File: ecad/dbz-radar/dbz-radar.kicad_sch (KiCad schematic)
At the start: 139 parts, among them J1 B2B-PH-SM4-TB, J2 USB4220-03-0880-C, J3 F300-1B7H1-11040-E100, J4 533980271, Q1 Q_PMOS, SW1 SW_Push, SW2 SW_Push, U1 USBLC6-2SC6, U2 TPS61169, U3 MCP738311/2, U4 MAX17048/9, U5 AP2112K-3.3, U6 PCA9554, U7 MAX98357A, U8 ESP32-S3-WROOM-1

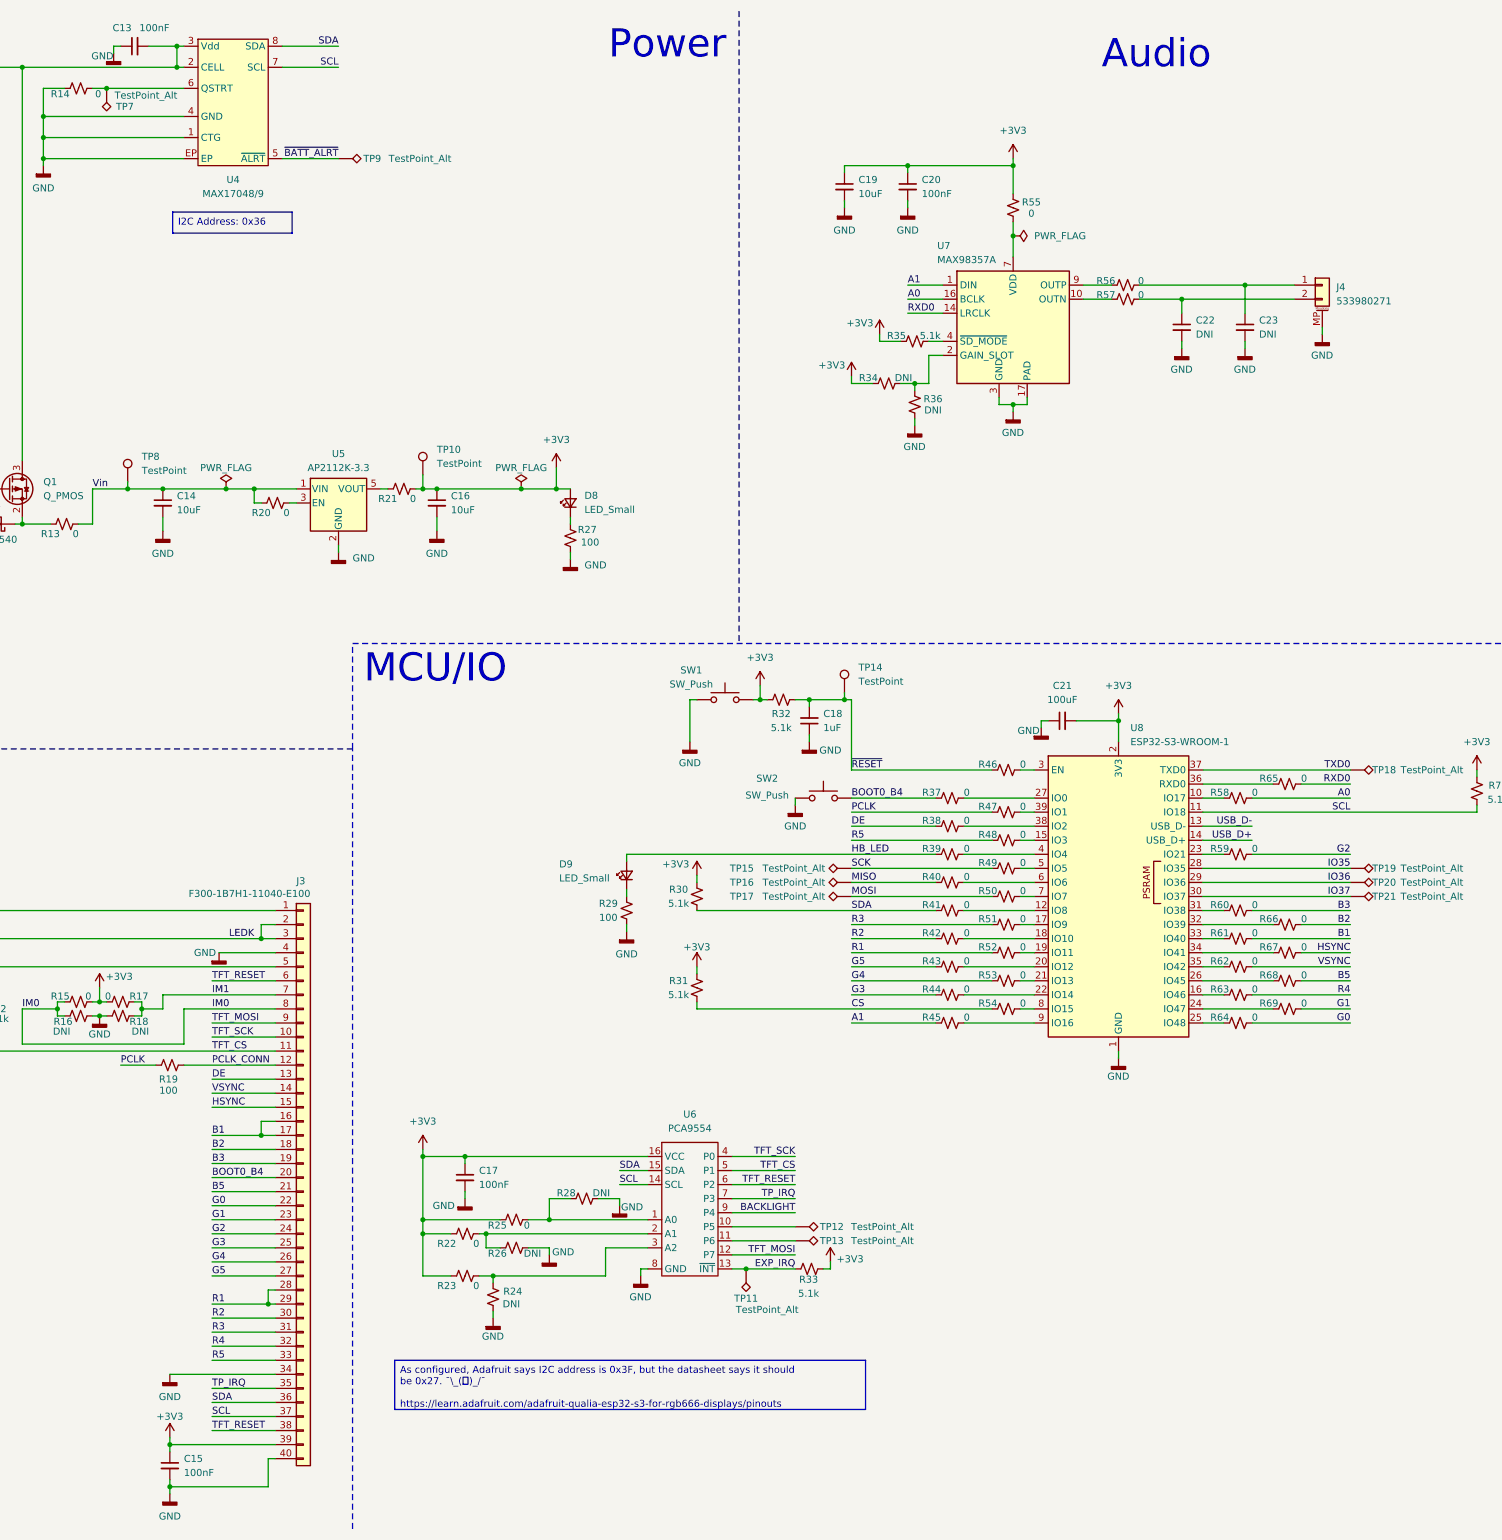
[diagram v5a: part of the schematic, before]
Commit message: added all footprints, some 3D models missing
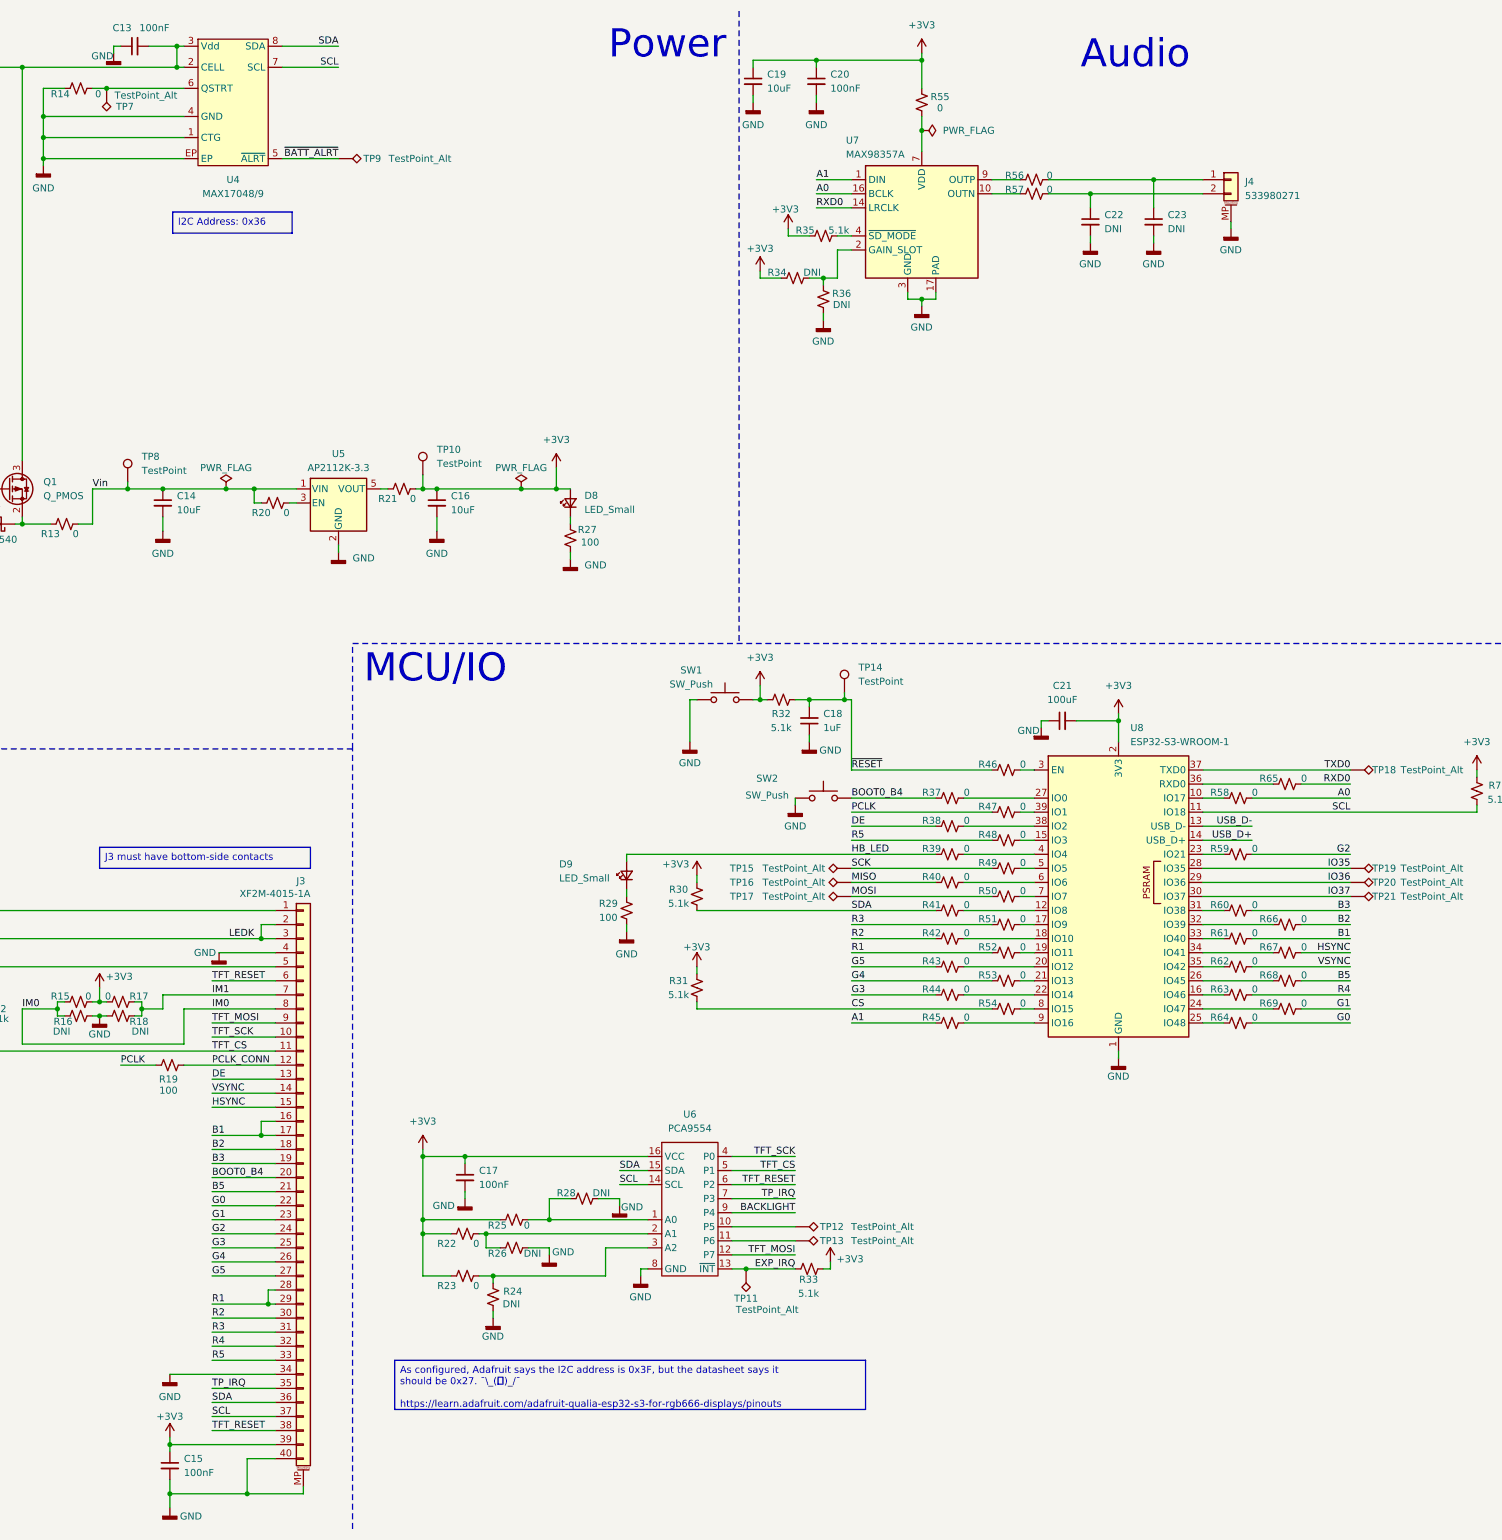
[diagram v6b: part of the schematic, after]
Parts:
- J3: value F300-1B7H1-11040-E100 -> XF2M-4015-1A; footprint (none) -> Connector_FFC-FPC:Omron_XF2M-4015-1A_1x40-1MP_P0.5mm_Horizontal; symbol Connector_Generic:Conn_01x40 -> Connector_Generic_MountingPin:Conn_01x40_MountingPin
- J4: footprint (none) -> Connector_Molex:Molex_PicoBlade_53398-0271_1x02-1MP_P1.25mm_Vertical
- U1: footprint Package_TO_SOT_SMD:SOT-23-6 -> Package_TO_SOT_SMD:SOT-23-6_Handsoldering
- U5: footprint Package_TO_SOT_SMD:SOT-23-5 -> Package_TO_SOT_SMD:SOT-23-5_HandSoldering
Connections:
- net GND: now also J3.MP (MountPin)
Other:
- moved on the sheet: C19, C20, C22, C23, J4, R34, R35, R36, R55, R56, R57, U7

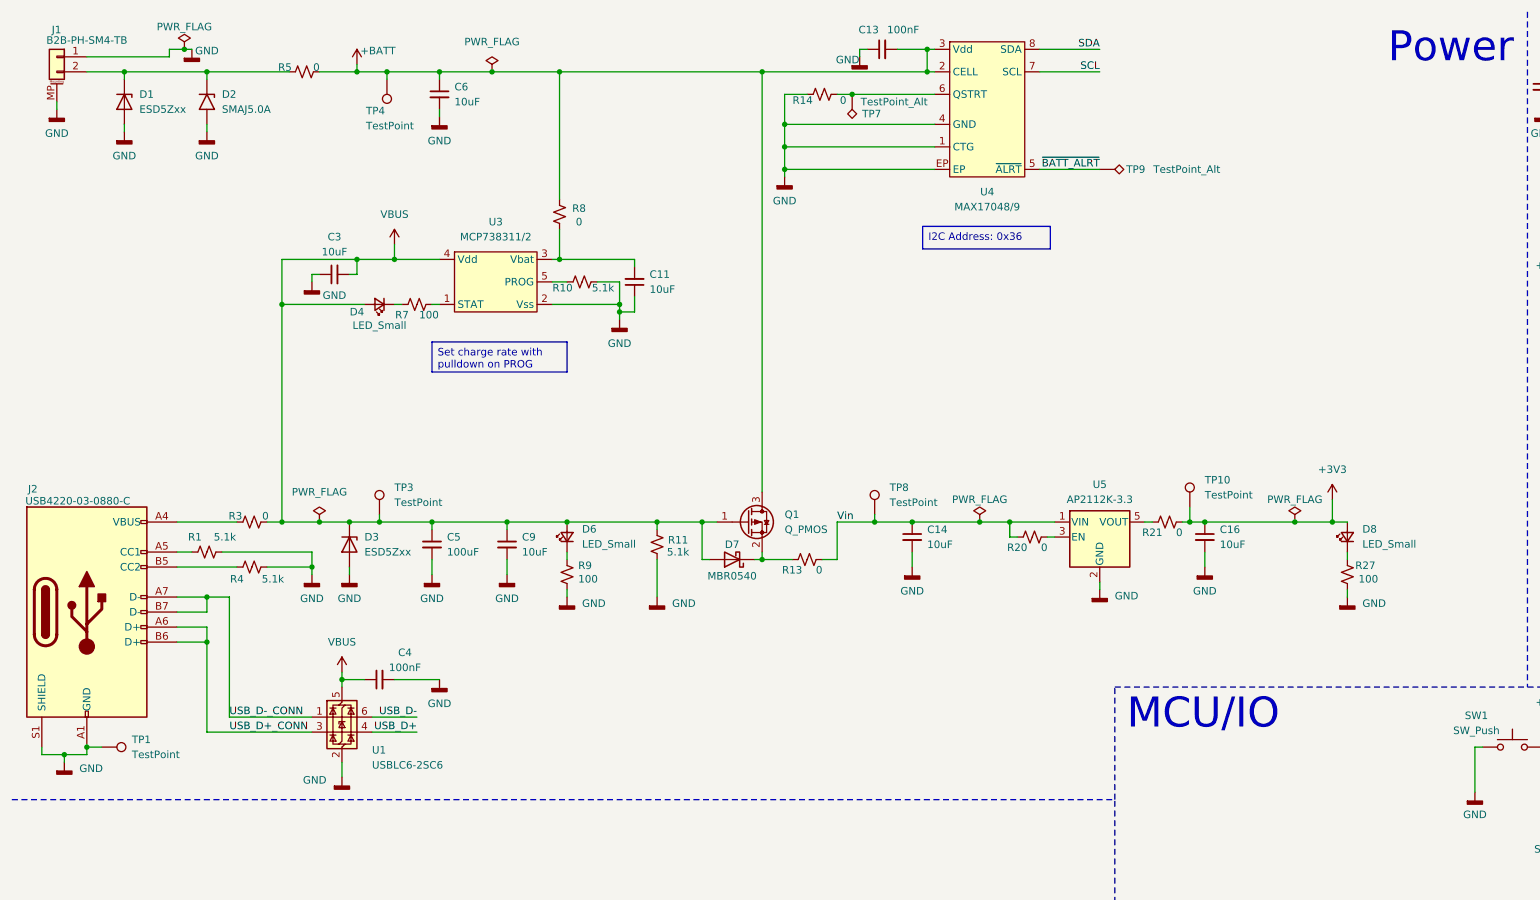
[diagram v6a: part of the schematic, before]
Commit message: match USB4220 symbol, footprint, and add 3D
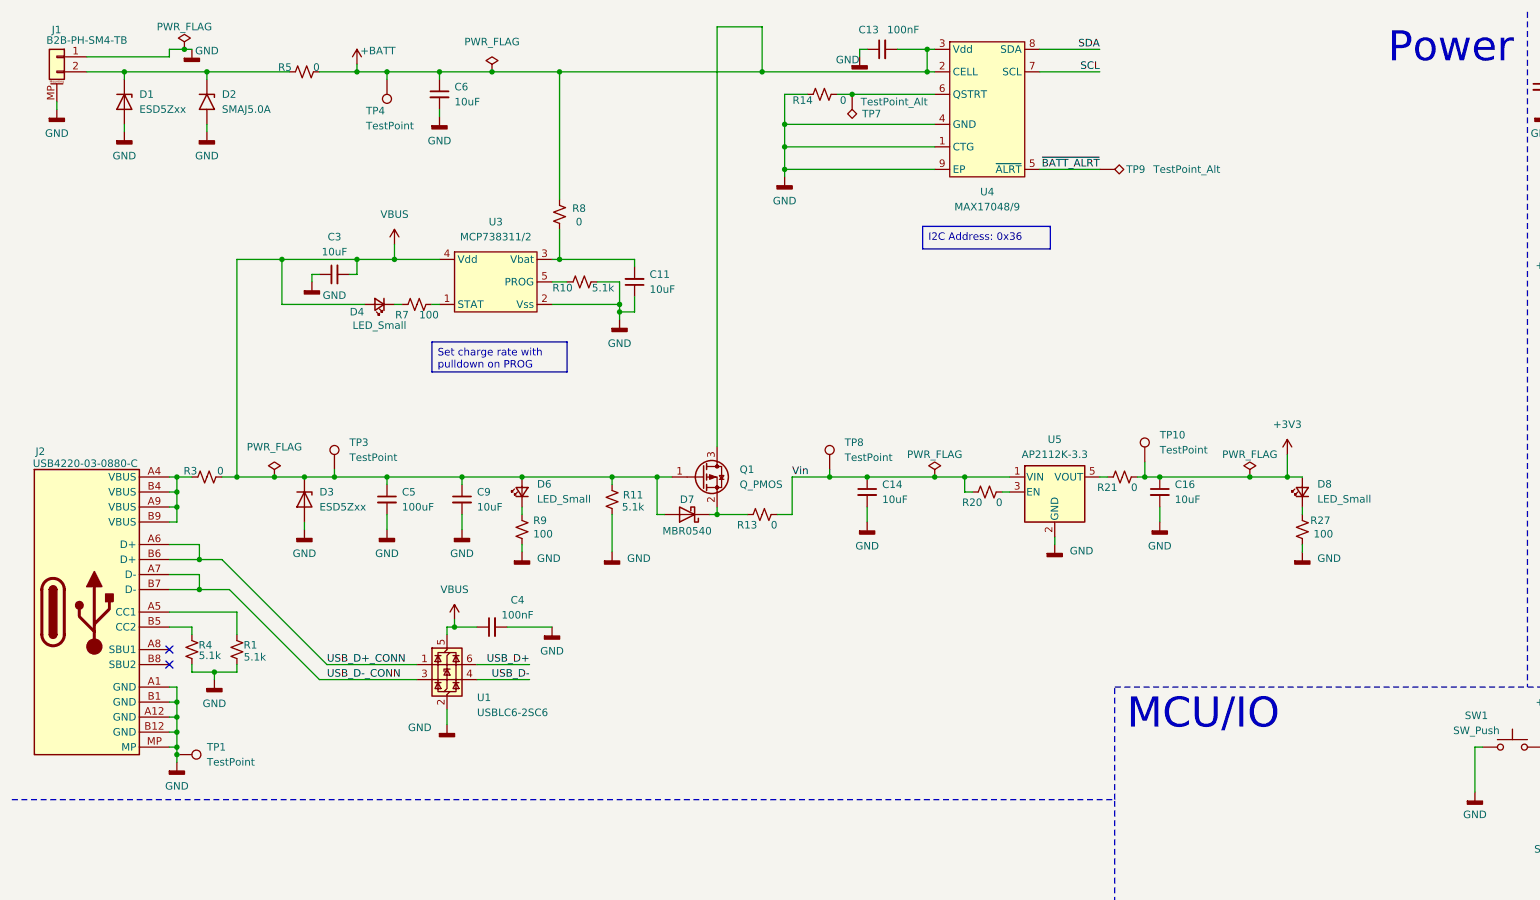
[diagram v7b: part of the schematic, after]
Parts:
- J2: symbol Connector:USB_C_Receptacle_USB2.0_14P -> USB4220-03:USB4220
- U2: footprint Package_TO_SOT_SMD:SOT-353_SC-70-5_Handsoldering -> Package_TO_SOT_SMD:SOT-353_SC-70-5
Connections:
- net GND: now also J2.MP, R1.1, R4.1, U4.9 (EP); no longer J2.S1 (SHIELD), R1.2, R4.2, U4.EP
- net USB_D+: now also U1.6 (I/O1); no longer U1.4 (I/O2)
- net USB_D+_CONN: now also U1.1 (I/O1); no longer U1.3 (I/O2)
- net USB_D-: now also U1.4 (I/O2); no longer U1.6 (I/O1)
- net USB_D-_CONN: now also U1.3 (I/O2); no longer U1.1 (I/O1)
- net at J2.B5 (CC2): now also R4.2; no longer R4.1
- net at J2.A5 (CC1): now also R1.2; no longer R1.1
- no-connect marks 0 -> 2
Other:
- moved on the sheet: C14, C16, C4, C5, C9, D3, D6, D7, D8, Q1, R1, R11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

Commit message: add user button symbol and footprints to layout
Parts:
- removed TP13: TestPoint_Alt, TestPoint:TestPoint_THTPad_D2.5mm_Drill1.2mm, symbol Connector:TestPoint_Alt
- added C24: 100nF, Capacitor_SMD:C_0805_2012Metric_Pad1.18x1.45mm_HandSolder, symbol Device:C_Small
- added FID1, FID2, FID3: Fiducial, Fiducial:Fiducial_1mm_Mask2mm, symbol Mechanical:Fiducial
- added H1, H2, H3, H4, H5, H6: MountingHole_Pad, M1:M1-mounting-hole, symbol Mechanical:MountingHole_Pad
- added R71: 5.1k, Resistor_SMD:R_0805_2012Metric_Pad1.20x1.40mm_HandSolder, symbol Device:R_Small_US
- added SW3: 1-825027-7, 1-825027-7:1-825027-7, symbol 1-825027-7:1-825027-7
- J1: footprint B2B-PH-SM4-TBLFSN_JST:B2B-PH-SM4-TB -> B2B-PH-SM4-TB:B2B-PH-SM4-TB
- J3: footprint Connector_FFC-FPC:Omron_XF2M-4015-1A_1x40-1MP_P0.5mm_Horizontal -> XF2M-4015-1A:XF2M-4015-1A
- SW1, SW2: value SW_Push -> SKRPACE010
- U4: footprint Package_DFN_QFN:DFN-8-1EP_2x2mm_P0.5mm_EP0.8x1.6mm -> MAX1704X:MAX1704X
- U7: footprint Package_DFN_QFN:TQFN-16-1EP_3x3mm_P0.5mm_EP1.23x1.23mm -> MAX98357XTEXX:MAX98357XTEXX
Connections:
- net +3V3: now also R71.2
- net GND: now also C24.2, H1.1, H2.1, H3.1, H4.1, H5.1, H6.1, SW3.1, SW3.MP
- net HB_LED: now also U6.10 (P5); no longer R39.1
- net at U6.11 (P6): now also TP12.1
- new net USER: C24.1, R39.1, R71.1, SW3.2
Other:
- moved on the sheet: D9, R29, TP12
